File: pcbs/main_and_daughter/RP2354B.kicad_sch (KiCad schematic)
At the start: 33 parts, among them J1 Conn_01x03_MountingPin, SW1 SW_Push, SW2 SW_Push, U2 RP2354B, Y1 ABM8-272-T3

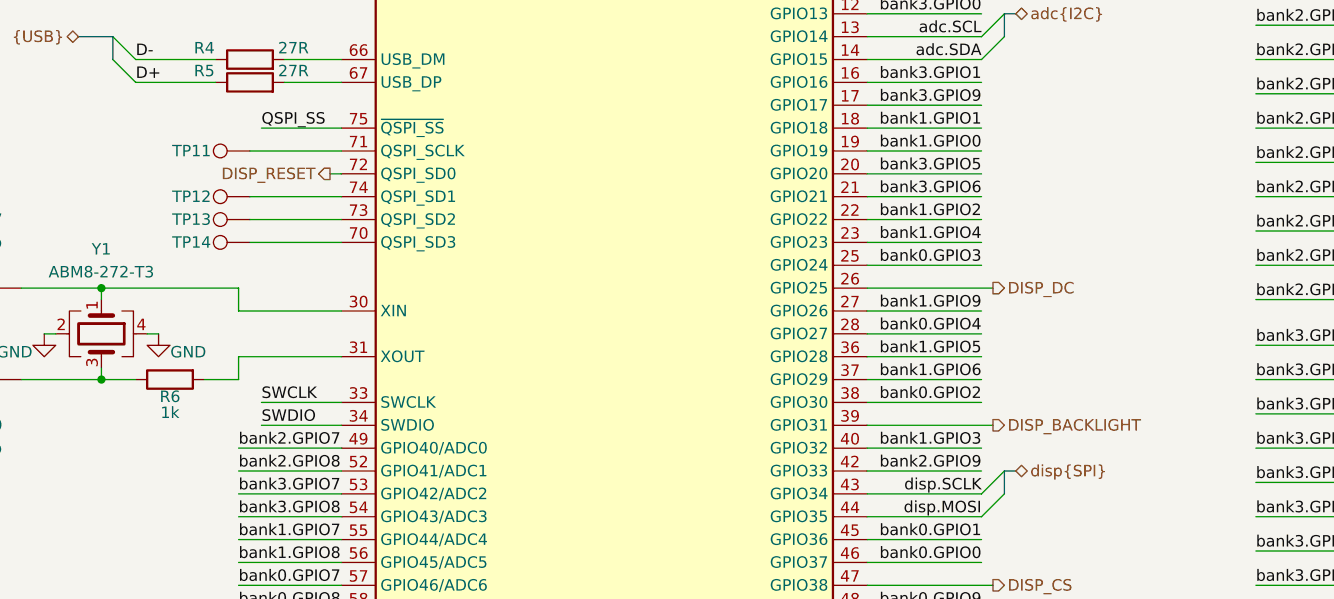
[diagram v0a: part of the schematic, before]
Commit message: removed display brightness control, ran out of pin
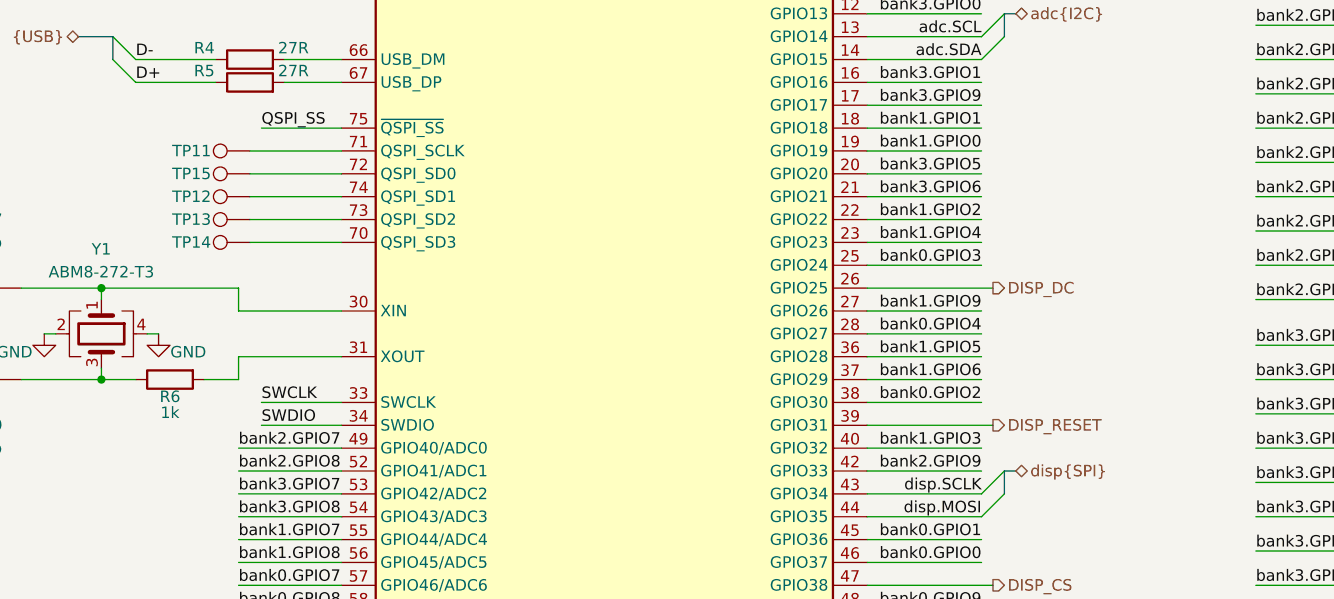
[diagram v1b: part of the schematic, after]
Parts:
- added TP15: TestPoint, TestPoint:TestPoint_Pad_D1.0mm, symbol Connector:TestPoint
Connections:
- net DISP_BACKLIGHT is gone; now on net DISP_RESET: U2.39 (GPIO31)
- net DISP_RESET: no longer U2.72 (QSPI_SD0)
- new net: TP15.1, U2.72 (QSPI_SD0)
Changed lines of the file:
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@@
 	(wire
 		(pts
+			(xy 81.28 102.87) (xy 91.44 102.87)
+		)
+		(stroke
+			(width 0)
+			(type default)
+		)
+	)
+	(wire
+		(pts
 			(xy 146.05 39.37) (xy 152.4 39.37)
 		)
@@
 	(wire
 		(pts
-			(xy 90.17 102.87) (xy 91.44 102.87)
-		)
-		(stroke
-			(width 0)
-			(type default)
-		)
-	)
-	(wire
-		(pts
 			(xy 198.12 25.4) (xy 199.39 25.4)
 		)
@@
 		)
 	)
-	(hierarchical_label "DISP_RESET"
-		(shape output)
-		(at 90.17 102.87 180)
-		(effects
-			(font
-				(size 1.27 1.27)
-			)
-			(justify right)
-		)
-	)
 	(hierarchical_label "bank1{GPIO_BANK}"
 		(shape bidirectional)
@@
 		)
 	)
-	(hierarchical_label "DISP_BACKLIGHT"
+	(hierarchical_label "DISP_RESET"
 		(shape output)
 		(at 163.83 130.81 0)
@@
 					(unit 1)
 				)
+			)
+		)
+	)
+	(symbol
+		(lib_id "Connector:TestPoint")
+		(at 81.28 102.87 90)
+		(unit 1)
+		(body_style 1)
+		(exclude_from_sim no)
+		(in_bom yes)
+		(on_board yes)
+		(in_pos_files yes)
+		(dnp no)
+		(property "Reference" "TP15"
+			(at 76.962 102.87 90)
+			(show_name no)
+			(do_not_autoplace no)
+			(effects
+				(font
+					(size 1.27 1.27)
+				)
+				(justify left)
+			)
+		)
+		(property "Value" "TestPoint"
+			(at 79.2479 100.33 0)
+			(hide yes)
+			(show_name no)
+			(do_not_autoplace no)
+			(effects
+				(font
+					(size 1.27 1.27)
+				)
+				(justify left)
+			)
+		)
+		(property "Footprint" "TestPoint:TestPoint_Pad_D1.0mm"
+			(at 81.28 97.79 0)
+			(hide yes)
+			(show_name no)
+			(do_not_autoplace no)
+			(effects
+				(font
+					(size 1.27 1.27)
+				)
+			)
+		)
+		(property "Datasheet" ""
+			(at 81.28 97.79 0)
+			(hide yes)
+			(show_name no)
+			(do_not_autoplace no)
+			(effects
+				(font
+					(size 1.27 1.27)
+				)
+			)
+		)
+		(property "Description" "test point"
+			(at 81.28 102.87 0)
+			(hide yes)
+			(show_name no)
+			(do_not_autoplace no)
+			(effects
+				(font
+					(size 1.27 1.27)
+				)
+			)
+		)
+		(pin "1"
+		)
+		(instances
+			(project "hackxpansion"
+				(path "/aaf5804d-3f78-442b-969e-39faa388db94/61af021d-ad04-487f-9d02-e2b100ecd1ae/77d1a66a-1629-4487-9557-00ea9a578a7b"
+					(reference "TP15")
+					(unit 1)
+				)

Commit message: added titles to schematic
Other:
- title: (none) -> RP2354B
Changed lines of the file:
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@@
 	(generator_version "10.0")
 	(paper "A4")
+	(title_block
+		(title "RP2354B")
+	)
 	(rectangle
 		(start 189.23 13.97)

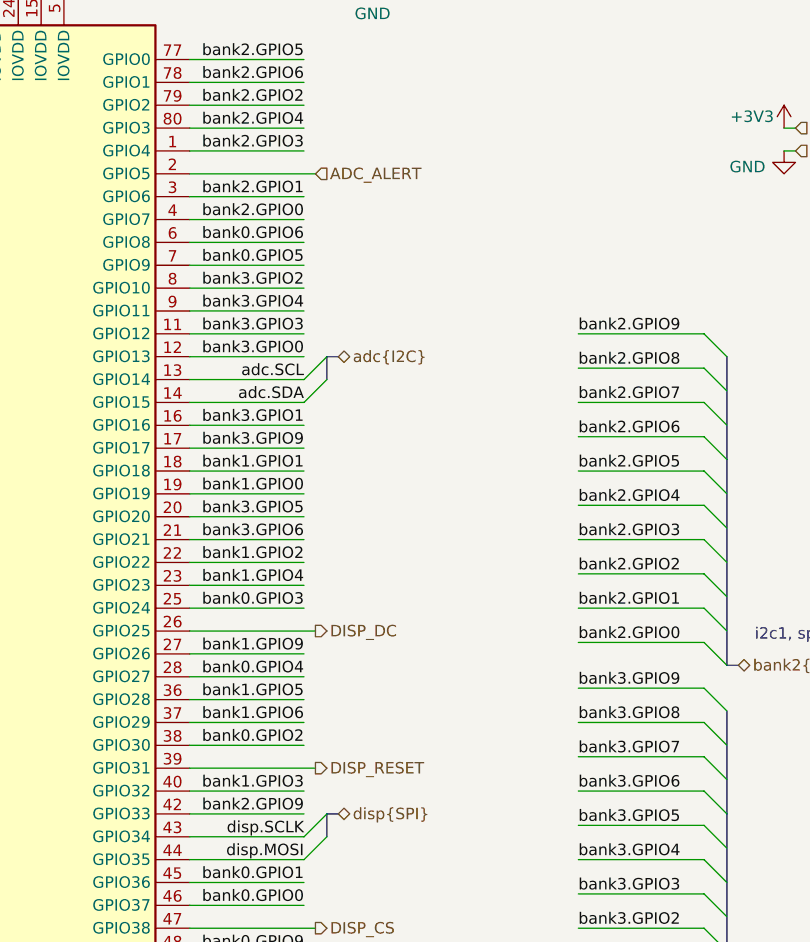
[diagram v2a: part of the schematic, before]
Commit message: added back display brightness, removed adc allert on pcb
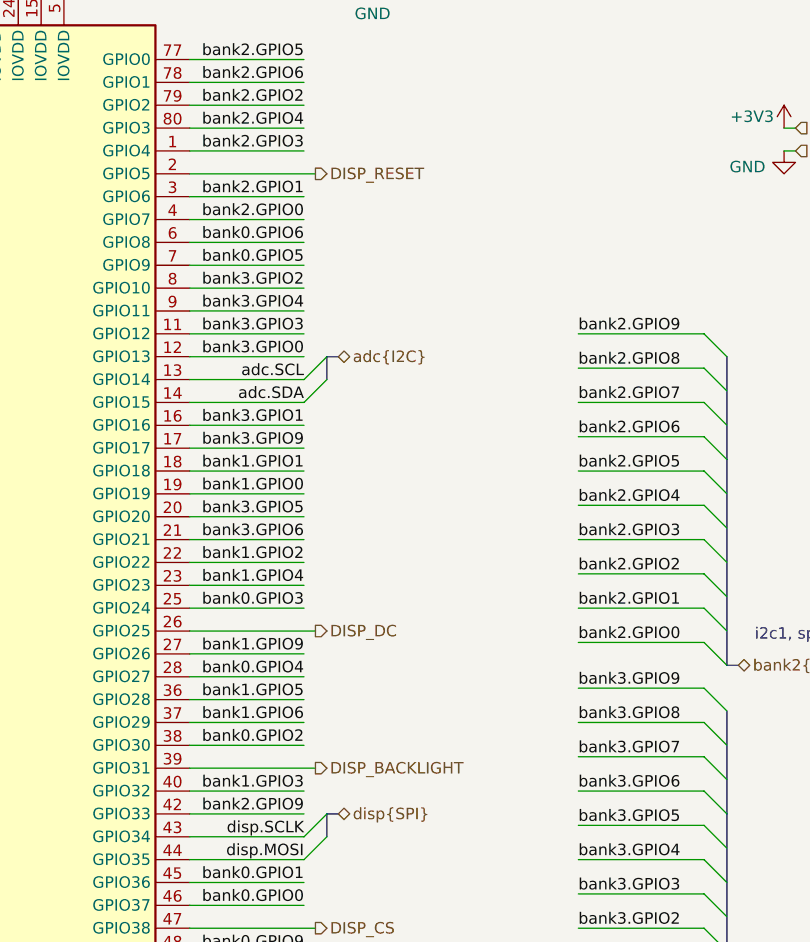
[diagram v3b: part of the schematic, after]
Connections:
- net ADC_ALERT is gone; now on net DISP_RESET: U2.2 (GPIO5)
- net DISP_RESET: no longer U2.39 (GPIO31)
- new net DISP_BACKLIGHT: U2.39 (GPIO31)
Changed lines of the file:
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@@
 	(wire
 		(pts
-			(xy 81.28 102.87) (xy 91.44 102.87)
-		)
-		(stroke
-			(width 0)
-			(type default)
-		)
-	)
-	(wire
-		(pts
 			(xy 146.05 39.37) (xy 152.4 39.37)
 		)
@@
 	(wire
 		(pts
+			(xy 81.28 102.87) (xy 91.44 102.87)
+		)
+		(stroke
+			(width 0)
+			(type default)
+		)
+	)
+	(wire
+		(pts
 			(xy 149.86 125.73) (xy 162.56 125.73)
 		)
@@
 		)
 	)
+	(hierarchical_label "DISP_RESET"
+		(shape output)
+		(at 163.83 64.77 0)
+		(effects
+			(font
+				(size 1.27 1.27)
+			)
+			(justify left)
+		)
+	)
 	(hierarchical_label "bank1{GPIO_BANK}"
 		(shape bidirectional)
@@
 		)
 	)
-	(hierarchical_label "DISP_RESET"
+	(hierarchical_label "DISP_BACKLIGHT"
 		(shape output)
 		(at 163.83 130.81 0)
@@
 		)
 	)
-	(hierarchical_label "ADC_ALERT"
-		(shape input)
-		(at 163.83 64.77 0)
-		(effects
-			(font
-				(size 1.27 1.27)
-			)
-			(justify left)
-		)
-	)
 	(hierarchical_label "disp{SPI}"
 		(shape bidirectional)
@@
 	)
 	(symbol
-		(lib_id "Connector:TestPoint")
-		(at 81.28 102.87 90)
-		(unit 1)
-		(body_style 1)
-		(exclude_from_sim no)
-		(in_bom yes)
-		(on_board yes)
-		(in_pos_files yes)
-		(dnp no)
-		(property "Reference" "TP15"
-			(at 76.962 102.87 90)
-			(show_name no)
-			(do_not_autoplace no)
-			(effects
-				(font
-					(size 1.27 1.27)
-				)
-				(justify left)
-			)
-		)
-		(property "Value" "TestPoint"
-			(at 79.2479 100.33 0)
-			(hide yes)
-			(show_name no)
-			(do_not_autoplace no)
-			(effects
-				(font
-					(size 1.27 1.27)
-				)
-				(justify left)
-			)
-		)
-		(property "Footprint" "TestPoint:TestPoint_Pad_D1.0mm"
-			(at 81.28 97.79 0)
-			(hide yes)
-			(show_name no)
-			(do_not_autoplace no)
-			(effects
-				(font
-					(size 1.27 1.27)
-				)
-			)
-		)
-		(property "Datasheet" ""
-			(at 81.28 97.79 0)
-			(hide yes)
-			(show_name no)
-			(do_not_autoplace no)
-			(effects
-				(font
-					(size 1.27 1.27)
-				)
-			)
-		)
-		(property "Description" "test point"
-			(at 81.28 102.87 0)
-			(hide yes)
-			(show_name no)
-			(do_not_autoplace no)
-			(effects
-				(font
-					(size 1.27 1.27)
-				)
-			)
-		)
-		(pin "1"
-		)
-		(instances
-			(project "hackxpansion"
-				(path "/aaf5804d-3f78-442b-969e-39faa388db94/61af021d-ad04-487f-9d02-e2b100ecd1ae/77d1a66a-1629-4487-9557-00ea9a578a7b"
-					(reference "TP15")
-					(unit 1)
-				)
-			)
-		)
-	)
-	(symbol
 		(lib_id "power:GND")
 		(at 63.5 52.07 0)
@@
 					(unit 1)
 				)
+			)
+		)
+	)
+	(symbol
+		(lib_id "Connector:TestPoint")
+		(at 81.28 102.87 90)
+		(unit 1)
+		(body_style 1)
+		(exclude_from_sim no)
+		(in_bom yes)
+		(on_board yes)
+		(in_pos_files yes)
+		(dnp no)
+		(property "Reference" "TP15"
+			(at 76.962 102.87 90)
+			(show_name no)
+			(do_not_autoplace no)
+			(effects
+				(font
+					(size 1.27 1.27)
+				)
+				(justify left)
+			)
+		)
+		(property "Value" "TestPoint"
+			(at 79.2479 100.33 0)
+			(hide yes)
+			(show_name no)
+			(do_not_autoplace no)
+			(effects
+				(font
+					(size 1.27 1.27)
+				)
+				(justify left)
+			)
+		)
+		(property "Footprint" "TestPoint:TestPoint_Pad_D1.0mm"
+			(at 81.28 97.79 0)
+			(hide yes)
+			(show_name no)
+			(do_not_autoplace no)
+			(effects
+				(font
+					(size 1.27 1.27)
+				)
+			)
+		)
+		(property "Datasheet" ""
+			(at 81.28 97.79 0)
+			(hide yes)
+			(show_name no)
+			(do_not_autoplace no)
+			(effects
+				(font
+					(size 1.27 1.27)
+				)
+			)
+		)
+		(property "Description" "test point"
+			(at 81.28 102.87 0)
+			(hide yes)
+			(show_name no)
+			(do_not_autoplace no)
+			(effects
+				(font
+					(size 1.27 1.27)
+				)
+			)
+		)
+		(pin "1"
+		)
+		(instances
+			(project "hackxpansion"
+				(path "/aaf5804d-3f78-442b-969e-39faa388db94/61af021d-ad04-487f-9d02-e2b100ecd1ae/77d1a66a-1629-4487-9557-00ea9a578a7b"
+					(reference "TP15")
+					(unit 1)
+				)

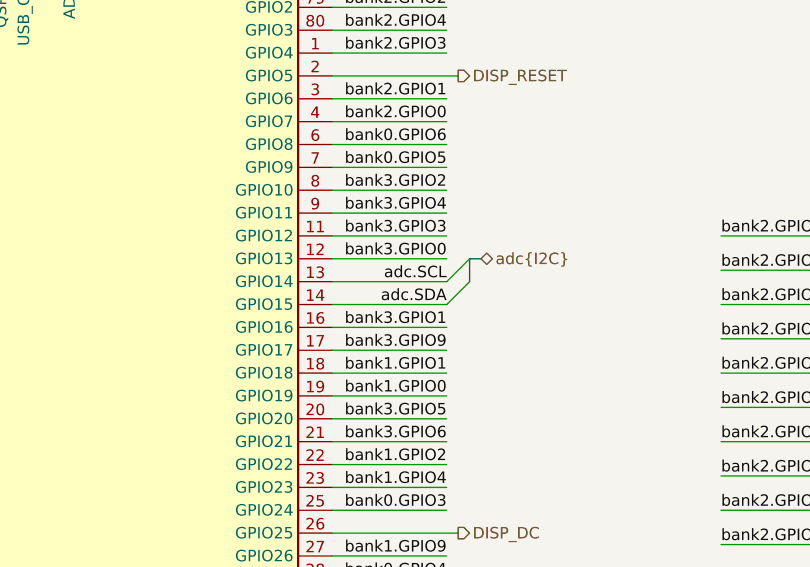
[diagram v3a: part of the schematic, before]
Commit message: switched the two i2c pins on the rpi for the adc
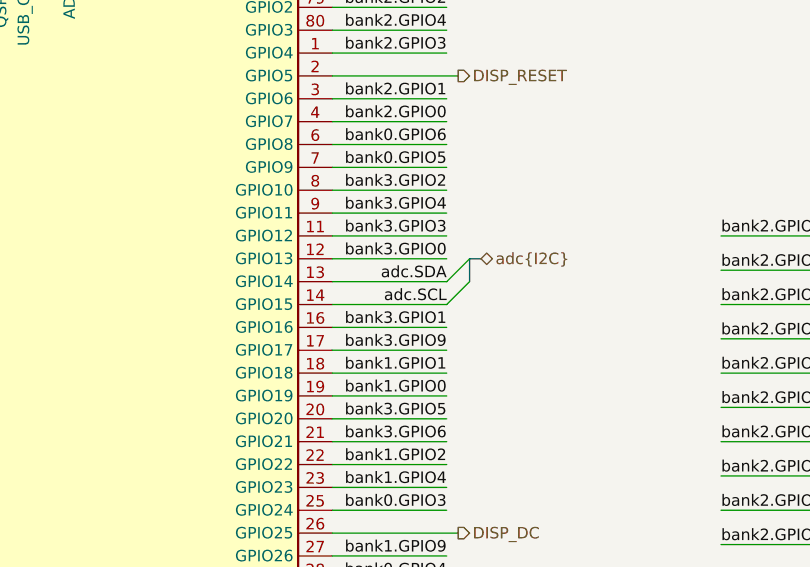
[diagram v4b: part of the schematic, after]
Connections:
- net adc.SCL: now also U2.14 (GPIO15); no longer U2.13 (GPIO14)
- net adc.SDA: now also U2.13 (GPIO14); no longer U2.14 (GPIO15)
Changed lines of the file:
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@@
 	)
 	(label "adc.SCL"
-		(at 162.56 87.63 180)
+		(at 162.56 90.17 180)
 		(effects
 			(font
@@
 	)
 	(label "adc.SDA"
-		(at 162.56 90.17 180)
+		(at 162.56 87.63 180)
 		(effects
 			(font

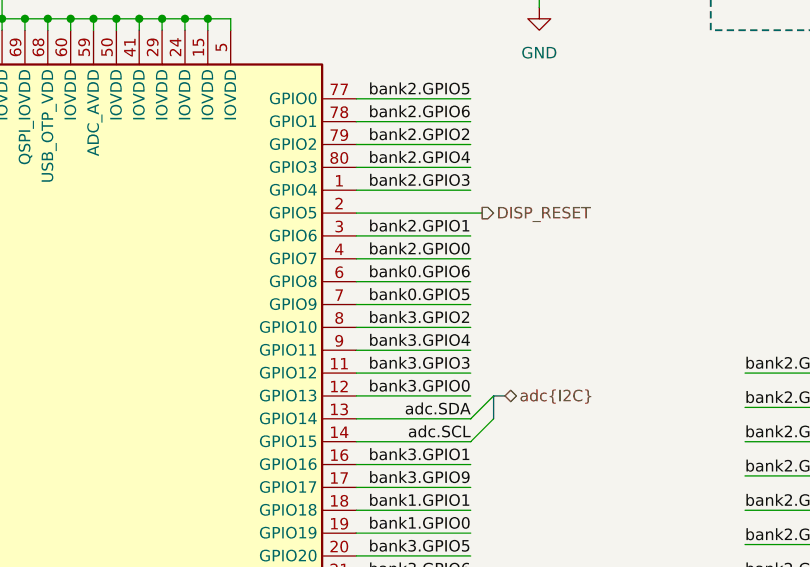
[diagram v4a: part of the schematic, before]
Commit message: switcheed bank 0 pin 5 and 6 cuz i messed up
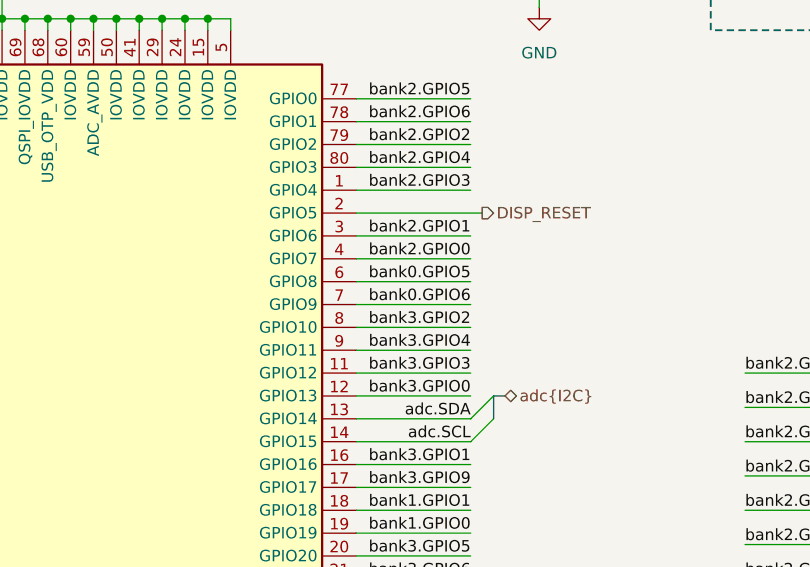
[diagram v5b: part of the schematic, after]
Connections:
- net bank0.GPIO5: now also U2.6 (GPIO8); no longer U2.7 (GPIO9)
- net bank0.GPIO6: now also U2.7 (GPIO9); no longer U2.6 (GPIO8)
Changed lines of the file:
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@@
 	)
 	(label "bank0.GPIO6"
-		(at 162.56 72.39 180)
+		(at 162.56 74.93 180)
 		(effects
 			(font
@@
 	)
 	(label "bank0.GPIO5"
-		(at 162.56 74.93 180)
+		(at 162.56 72.39 180)
 		(effects
 			(font

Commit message: added lcsc part nums
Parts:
- C1, C10, C11, C12, C3, C4, C5, C6, C7, C8, C9: LCSC (none) -> C1525
- C14, C2: LCSC (none) -> C23733
- C15, C16: LCSC (none) -> C52923
- C17, C19: LCSC (none) -> C1548
- J1: LCSC (none) -> C160403
- L1: LCSC (none) -> C42411119
- R1, R3, R6: LCSC (none) -> C11702
- R2: LCSC (none) -> C25105
- R4, R5: LCSC (none) -> C2909343
- SW1, SW2: LCSC (none) -> C231329
- TP11, TP12, TP13, TP14, TP15: now left out of the parts list
- U2: LCSC (none) -> C39843328
- Y1: LCSC (none) -> 5A992C

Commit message: updated bom and lcsc part nums
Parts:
- R4, R5: LCSC C2909343 -> C2929914
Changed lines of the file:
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@@
 			)
 		)
-		(property "LCSC" "C2909343"
+		(property "LCSC" "C2929914"
 			(at 81.28 92.71 90)
 			(hide yes)
@@
 			)
 		)
-		(property "LCSC" "C2909343"
+		(property "LCSC" "C2929914"
 			(at 81.28 90.17 90)
 			(hide yes)
